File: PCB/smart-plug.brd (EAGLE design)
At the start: 85.1 x 77.1 mm, 10 parts, among them K1 HLS8L-DC3V-S-C, T1 2N2222

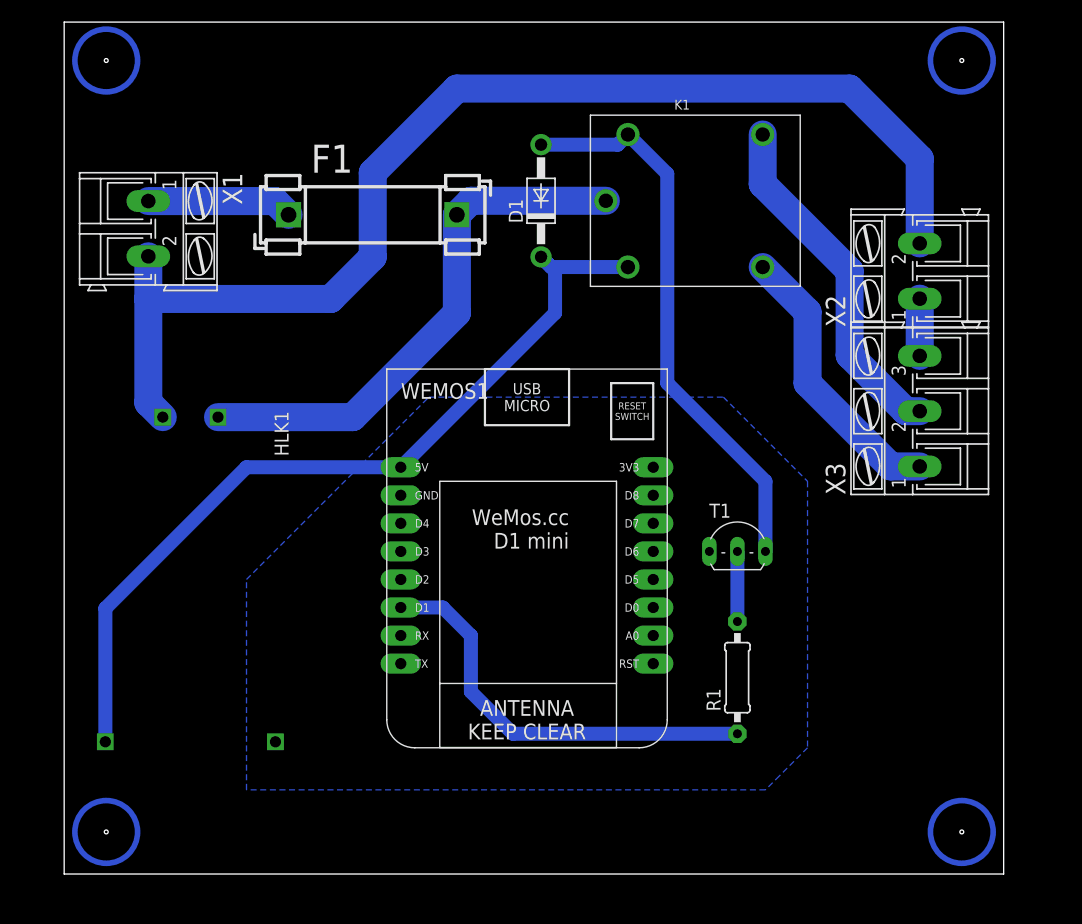
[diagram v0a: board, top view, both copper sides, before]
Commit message: Update files
Added LED indicators
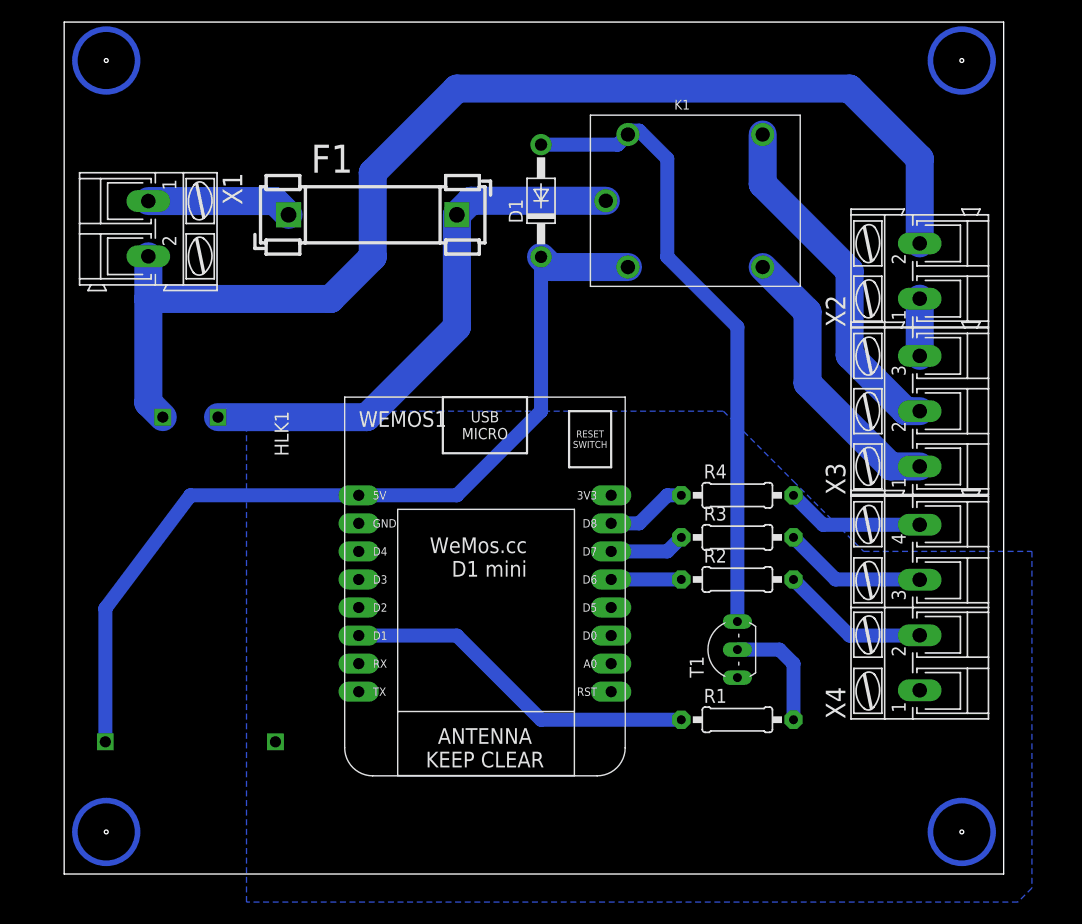
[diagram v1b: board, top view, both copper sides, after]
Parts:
- added R2, R3, R4: (no value), adafruit:0207/10
- added X4: (no value), con-ptr500:AK300/4
- moved T1 10.2 mm to (68.6, 20.3), turned to 90 degrees
- moved WEMOS1 4.58 mm to (48.3, 24.1)
- moved R1 3.81 mm to (69.8, 14.0), turned to 0 degrees
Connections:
- new net LED_BLUE: R4.1, WEMOS1.D8
- new net LED_GREEN: R3.1, WEMOS1.D7
- new net LED_RED: R2.1, WEMOS1.D6
- new net N$10: R4.2, X4.4
- new net N$11: R3.2, X4.3
- new net N$9: R2.2, X4.2
- net AGND: now also X4.1
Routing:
- net N$9: track 0.00 -> 13.5 mm
- net N$11: track 0.00 -> 13.0 mm
- net N$10: track 0.00 -> 12.5 mm
- net LED_BLUE: track 0.00 -> 7.40 mm
- net LED_GREEN: track 0.00 -> 6.88 mm
- net N$6: track 51.2 -> 57.5 mm
- net LED_RED: track 0.00 -> 6.35 mm
- net N$2: track 38.2 -> 32.4 mm
- net N$3: track 6.35 -> 10.7 mm
- net N$4: track 77.7 -> 82.0 mm
- net 220V+: track 48.4 -> 49.2 mm
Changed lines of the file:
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@@
 <attribute name="MPN" value="HLS8L-DC3V-S-C" x="66.04" y="60.96" size="1.778" layer="27" display="off"/>
 </element>
-<element name="R1" library="adafruit" package="0207/10" value="" x="69.85" y="17.78" rot="R90"/>
-<element name="T1" library="adafruit" package="TO92-EBC-OVAL" value="2N2222" x="69.85" y="30.48"/>
-<element name="WEMOS1" library="esp8266modules" package="WEMOS-D1-MINI" value="" x="52.07" y="26.67" rot="R180"/>
+<element name="R1" library="adafruit" package="0207/10" value="" x="69.85" y="13.97"/>
+<element name="T1" library="adafruit" package="TO92-EBC-OVAL" value="2N2222" x="68.58" y="20.32" rot="R90"/>
+<element name="WEMOS1" library="esp8266modules" package="WEMOS-D1-MINI" value="" x="48.26" y="24.13" rot="R180"/>
 <element name="X1" library="con-ptr500" library_urn="urn:adsk.eagle:library:181" package="AK300/2" package3d_urn="urn:adsk.eagle:package:9881/1" value="" x="16.51" y="58.42" rot="R270">
 <attribute name="MF" value="" x="16.51" y="58.42" size="1.778" layer="27" rot="R270" display="off"/>
@@
 <attribute name="OC_NEWARK" value="unknown" x="29.21" y="59.69" size="1.778" layer="27" display="off"/>
 </element>
+<element name="R2" library="adafruit" package="0207/10" value="" x="69.85" y="26.67"/>
+<element name="R3" library="adafruit" package="0207/10" value="" x="69.85" y="30.48"/>
+<element name="R4" library="adafruit" package="0207/10" value="" x="69.85" y="34.29"/>
+<element name="X4" library="con-ptr500" library_urn="urn:adsk.eagle:library:181" package="AK300/4" package3d_urn="urn:adsk.eagle:package:9879/1" value="" x="86.36" y="24.13" rot="R90">
+<attribute name="MF" value="" x="86.36" y="24.13" size="1.778" layer="27" rot="R90" display="off"/>
+<attribute name="MPN" value="" x="86.36" y="24.13" size="1.778" layer="27" rot="R90" display="off"/>
+<attribute name="OC_FARNELL" value="unknown" x="86.36" y="24.13" size="1.778" layer="27" rot="R90" display="off"/>
+<attribute name="OC_NEWARK" value="unknown" x="86.36" y="24.13" size="1.778" layer="27" rot="R90" display="off"/>
+</element>
 </elements>
 <signals>
-<signal name="N$2">
-<contactref element="WEMOS1" pad="D1"/>
-<contactref element="R1" pad="1"/>
-<wire x1="39.37" y1="24.13" x2="43.18" y2="24.13" width="1.27" layer="16"/>
-<wire x1="43.18" y1="24.13" x2="45.72" y2="21.59" width="1.27" layer="16"/>
-<wire x1="45.72" y1="21.59" x2="45.72" y2="16.51" width="1.27" layer="16"/>
-<wire x1="45.72" y1="16.51" x2="49.53" y2="12.7" width="1.27" layer="16"/>
-<wire x1="49.53" y1="12.7" x2="69.85" y2="12.7" width="1.27" layer="16"/>
-</signal>
 <signal name="N$3">
 <contactref element="R1" pad="2"/>
 <contactref element="T1" pad="B"/>
-<wire x1="69.85" y1="22.86" x2="69.85" y2="29.21" width="1.27" layer="16"/>
+<wire x1="69.85" y1="20.32" x2="73.66" y2="20.32" width="1.27" layer="16"/>
+<wire x1="73.66" y1="20.32" x2="74.93" y2="19.05" width="1.27" layer="16"/>
+<wire x1="74.93" y1="19.05" x2="74.93" y2="13.97" width="1.27" layer="16"/>
 </signal>
 <signal name="N$4">
@@
 <contactref element="WEMOS1" pad="5V"/>
 <contactref element="HLK1" pad="P$4"/>
-<wire x1="52.07" y1="55.88" x2="52.99" y2="54.96" width="1.27" layer="16"/>
-<wire x1="52.99" y1="54.96" x2="59.94" y2="54.96" width="1.27" layer="16"/>
-<wire x1="39.37" y1="36.83" x2="53.34" y2="50.8" width="1.27" layer="16"/>
-<wire x1="53.34" y1="50.8" x2="53.34" y2="54.61" width="1.27" layer="16"/>
-<wire x1="53.34" y1="54.61" x2="52.07" y2="55.88" width="1.27" layer="16"/>
 <wire x1="12.62" y1="11.97" x2="12.62" y2="24.05" width="1.27" layer="16"/>
-<wire x1="25.4" y1="36.83" x2="39.37" y2="36.83" width="1.27" layer="16"/>
-<wire x1="12.62" y1="24.05" x2="25.4" y2="36.83" width="1.27" layer="16"/>
+<wire x1="12.62" y1="24.05" x2="20.32" y2="34.29" width="1.27" layer="16"/>
+<wire x1="20.32" y1="34.29" x2="35.56" y2="34.29" width="1.27" layer="16"/>
+<wire x1="35.56" y1="34.29" x2="44.45" y2="34.29" width="1.27" layer="16"/>
+<wire x1="44.45" y1="34.29" x2="52.07" y2="41.91" width="1.27" layer="16"/>
+<wire x1="52.07" y1="41.91" x2="52.07" y2="55.88" width="1.27" layer="16"/>
+<wire x1="52.07" y1="55.88" x2="52.99" y2="54.96" width="2.54" layer="16"/>
+<wire x1="52.99" y1="54.96" x2="59.94" y2="54.96" width="2.54" layer="16"/>
 </signal>
 <signal name="AGND">
@@
 <contactref element="WEMOS1" pad="GND"/>
 <contactref element="HLK1" pad="P$3"/>
+<contactref element="X4" pad="1"/>
 <polygon width="0.508" layer="16">
-<vertex x="25.4" y="7.62"/>
-<vertex x="25.4" y="26.67"/>
-<vertex x="41.91" y="43.18"/>
-<vertex x="68.58" y="43.18"/>
-<vertex x="76.2" y="35.56"/>
-<vertex x="76.2" y="11.43"/>
-<vertex x="73.66" y="8.89"/>
-<vertex x="72.39" y="7.62"/>
+<vertex x="25.4" y="41.91"/>
+<vertex x="68.58" y="41.91"/>
+<vertex x="74.93" y="35.56"/>
+<vertex x="81.28" y="29.21"/>
+<vertex x="96.52" y="29.21"/>
+<vertex x="96.52" y="-1.27"/>
+<vertex x="95.25" y="-2.54"/>
+<vertex x="25.4" y="-2.54"/>
 </polygon>
 </signal>
@@
 <wire x1="52.07" y1="66.04" x2="59.02" y2="66.04" width="1.27" layer="16"/>
 <wire x1="59.02" y1="66.04" x2="59.94" y2="66.96" width="1.27" layer="16"/>
-<wire x1="63.5" y1="63.4" x2="59.94" y2="66.96" width="1.27" layer="16"/>
-<wire x1="72.39" y1="29.21" x2="72.39" y2="35.56" width="1.27" layer="16"/>
-<wire x1="72.39" y1="35.56" x2="63.5" y2="44.45" width="1.27" layer="16"/>
-<wire x1="63.5" y1="44.45" x2="63.5" y2="63.4" width="1.27" layer="16"/>
+<wire x1="69.85" y1="49.53" x2="63.5" y2="55.88" width="1.27" layer="16"/>
+<wire x1="63.5" y1="55.88" x2="63.5" y2="64.77" width="1.27" layer="16"/>
+<wire x1="63.5" y1="64.77" x2="60.96" y2="67.31" width="1.27" layer="16"/>
+<wire x1="60.96" y1="67.31" x2="60.29" y2="67.31" width="1.27" layer="16"/>
+<wire x1="60.29" y1="67.31" x2="59.94" y2="66.96" width="1.27" layer="16"/>
+<wire x1="69.85" y1="22.86" x2="69.85" y2="49.53" width="1.27" layer="16"/>
 </signal>
 <signal name="220V+">
@@
 <contactref element="F1" pad="2"/>
 <contactref element="HLK1" pad="P$1"/>
-<wire x1="22.82" y1="41.37" x2="35.02" y2="41.37" width="2.54" layer="16"/>
-<wire x1="35.02" y1="41.37" x2="44.45" y2="50.8" width="2.54" layer="16"/>
-<wire x1="44.45" y1="50.8" x2="44.45" y2="59.69" width="2.54" layer="16"/>
 <wire x1="57.94" y1="60.96" x2="45.72" y2="60.96" width="2.54" layer="16"/>
 <wire x1="45.72" y1="60.96" x2="44.45" y2="59.69" width="2.54" layer="16"/>
+<wire x1="22.82" y1="41.37" x2="36.29" y2="41.37" width="2.54" layer="16"/>
+<wire x1="36.29" y1="41.37" x2="44.45" y2="49.53" width="2.54" layer="16"/>
+<wire x1="44.45" y1="49.53" x2="44.45" y2="59.69" width="2.54" layer="16"/>
 </signal>
 <signal name="220V-">
@@
 <wire x1="76.2" y1="44.45" x2="76.2" y2="50.9" width="2.54" layer="16"/>
 </signal>
+<signal name="LED_BLUE">
+<contactref element="WEMOS1" pad="D8"/>
+<contactref element="R4" pad="1"/>
+<wire x1="64.77" y1="34.29" x2="63.5" y2="34.29" width="1.27" layer="16"/>
+<wire x1="63.5" y1="34.29" x2="60.96" y2="31.75" width="1.27" layer="16"/>
+<wire x1="60.96" y1="31.75" x2="58.42" y2="31.75" width="1.27" layer="16"/>
+</signal>
+<signal name="LED_GREEN">
+<contactref element="WEMOS1" pad="D7"/>
+<contactref element="R3" pad="1"/>
+<wire x1="64.77" y1="30.48" x2="63.5" y2="29.21" width="1.27" layer="16"/>
+<wire x1="63.5" y1="29.21" x2="58.42" y2="29.21" width="1.27" layer="16"/>
+</signal>
+<signal name="LED_RED">
+<contactref element="WEMOS1" pad="D6"/>
+<contactref element="R2" pad="1"/>
+<wire x1="64.77" y1="26.67" x2="58.42" y2="26.67" width="1.27" layer="16"/>
+</signal>
+<signal name="N$2">
+<contactref element="WEMOS1" pad="D1"/>
+<contactref element="R1" pad="1"/>
+<wire x1="35.56" y1="21.59" x2="44.45" y2="21.59" width="1.27" layer="16"/>
+<wire x1="44.45" y1="21.59" x2="52.07" y2="13.97" width="1.27" layer="16"/>
+<wire x1="52.07" y1="13.97" x2="64.77" y2="13.97" width="1.27" layer="16"/>
+</signal>
+<signal name="N$11">
+<contactref element="X4" pad="3"/>
+<contactref element="R3" pad="2"/>
+<wire x1="86.36" y1="26.6446" x2="86.3346" y2="26.67" width="1.27" layer="16"/>
+<wire x1="78.74" y1="26.67" x2="74.93" y2="30.48" width="1.27" layer="16"/>
+<wire x1="86.3346" y1="26.67" x2="78.74" y2="26.67" width="1.27" layer="16"/>
+</signal>
+<signal name="N$9">
+<contactref element="X4" pad="2"/>
+<contactref element="R2" pad="2"/>
+<wire x1="74.93" y1="26.67" x2="80.01" y2="21.59" width="1.27" layer="16"/>
+<wire x1="80.01" y1="21.59" x2="86.3346" y2="21.59" width="1.27" layer="16"/>
+<wire x1="86.3346" y1="21.59" x2="86.36" y2="21.6154" width="1.27" layer="16"/>
+</signal>
+<signal name="N$10">
+<contactref element="X4" pad="4"/>
+<contactref element="R4" pad="2"/>
+<wire x1="86.36" y1="31.623" x2="77.597" y2="31.623" width="1.27" layer="16"/>
+<wire x1="77.597" y1="31.623" x2="74.93" y2="34.29" width="1.27" layer="16"/>
+</signal>
 </signals>

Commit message: Update files
Added on board LEDs, updated design
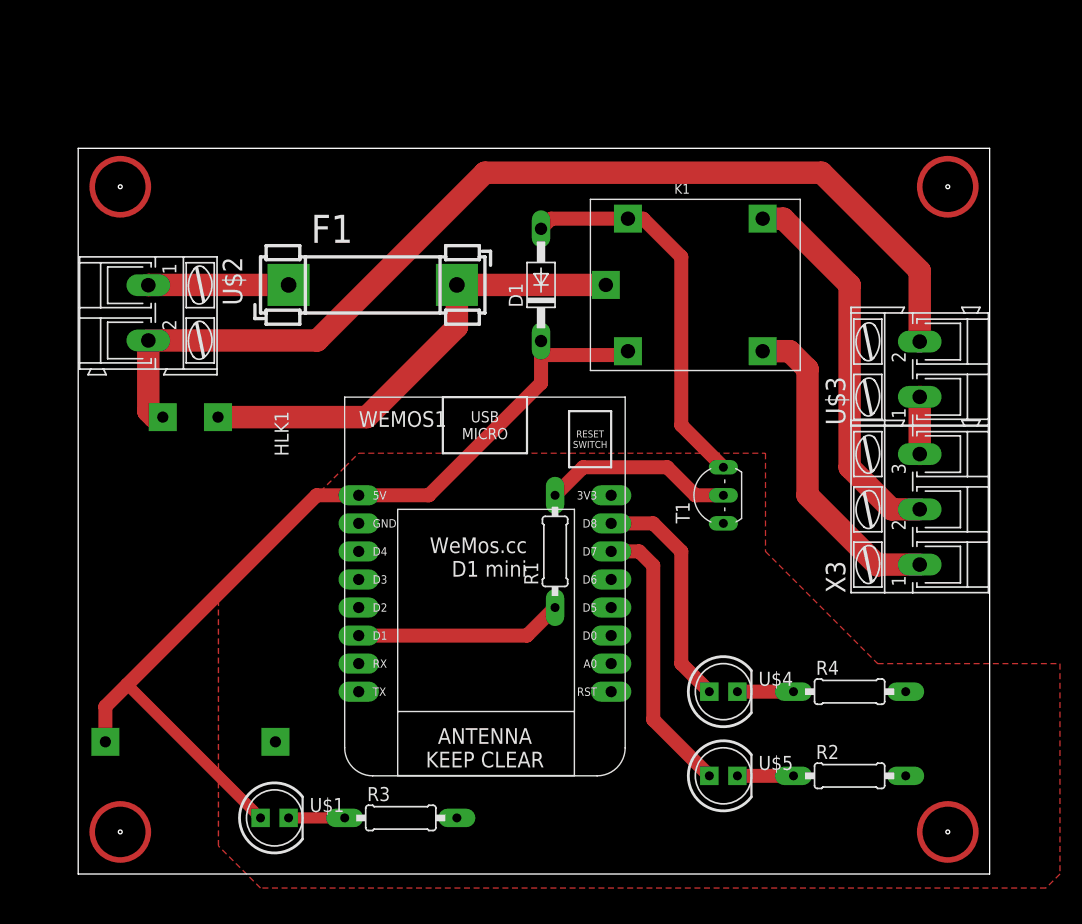
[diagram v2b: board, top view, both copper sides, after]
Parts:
- removed X1, X2: (no value), con-ptr500:AK300/2
- removed X4: (no value), con-ptr500:AK300/4
- added U$1, U$4, U$5: LED5MM, smartplug-components:LED5MM
- added U$2, U$3: OUT-2PINS, smartplug-components:AK300/2
- D1: value 1N4004 -> DIODE; device adafruit:DO41-10 -> smartplug-components:DO41-10
- F1: value FUSEBLANK_5X20MM -> FUSE-HOLDER; device fuse:FUSE_HOLDER_5X20MM -> smartplug-components:FUSE_HOLDER_5X20MM
- HLK1: value HLK-PM013W -> HLK-SUPPLY; device HLK-PM01:HLK-PM01 -> smartplug-components:HLK-PM01
- K1: device Seeed-Relay:REY5-19.0X15.0X15.0MM -> smartplug-components:REY5-19.0X15.0X15.0MM
- R1, R2, R3, R4: value (none) -> RESISTOR; device adafruit:0207/10 -> smartplug-components:0207/10
- WEMOS1: value (none) -> WEMOS-D1-MINI; device esp8266modules:WEMOS-D1-MINI -> smartplug-components:WEMOS-D1-MINI
- X3: value (none) -> OUT-3PINS; device con-ptr500:AK300/3 -> smartplug-components:AK300/3
- moved R3 39.7 mm to (39.4, 5.08)
- moved R1 22.5 mm to (53.3, 29.2), turned to 90 degrees
- moved R2 20.5 mm to (80.0, 8.89)
- moved R4 20.5 mm to (80.0, 16.5)
- moved T1 14.0 mm to (67.3, 34.3)
- moved X3 8.89 mm to (86.4, 33.0)
- moved D1 7.62 mm to (52.1, 53.3)
- moved K1 7.62 mm to (66.0, 53.3)
- moved F1 6.35 mm to (29.2, 53.3)
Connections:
- net N$5 renamed RELAY2
- net N$7 renamed RELAY1
- removed net N$1: X2.1, X3.3
- removed net N$11: R3.2, X4.3
- new net SWITCH: U$3.1, X3.3
- net 220V-: now also U$2.2, U$3.2; no longer X1.2, X2.2
- net AGND: now also R2.2, R3.2, R4.2; no longer X4.1
- net LED_BLUE: now also U$4.A; no longer R4.1
- net LED_GREEN: now also U$1.K; no longer WEMOS1.D7
- net LED_RED: now also U$5.A, WEMOS1.D7; no longer R2.1, WEMOS1.D6
- net N$10: now also R4.1, U$4.K; no longer R4.2, X4.4
- net N$4: now also U$1.A
- net N$8: now also U$2.1; no longer X1.1
- net N$9: now also R2.1, U$5.K; no longer R2.2, X4.2
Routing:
- net N$6: track 57.5 -> 35.1 mm
- net LED_RED: track 6.35 -> 25.5 mm
- net LED_BLUE: track 7.40 -> 21.2 mm
- net N$2: track 32.4 -> 18.8 mm
- net 220V-: track 107.6 -> 94.2 mm
- net N$11: track 13.0 -> 0.00 mm
- net N$9: track 13.5 -> 5.08 mm
- net N$10: track 12.5 -> 5.08 mm
- net 220V+: track 49.2 -> 42.3 mm
- net N$3: track 10.7 -> 17.3 mm
- net SWITCH: track 0.00 -> 5.18 mm
- net N$1: track 5.18 -> 0.00 mm
- net RELAY1: track 25.5 -> 29.0 mm
- net RELAY2: track 31.7 -> 34.8 mm
- net LED_GREEN: track 6.88 -> 5.08 mm
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- added copper zone on layer 1, net AGND
- removed copper zone on layer 16, net AGND
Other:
- board size 85.1 x 77.1 mm -> 82.5 x 65.7 mm

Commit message: Update files
Removed fuse and made PCB smaller
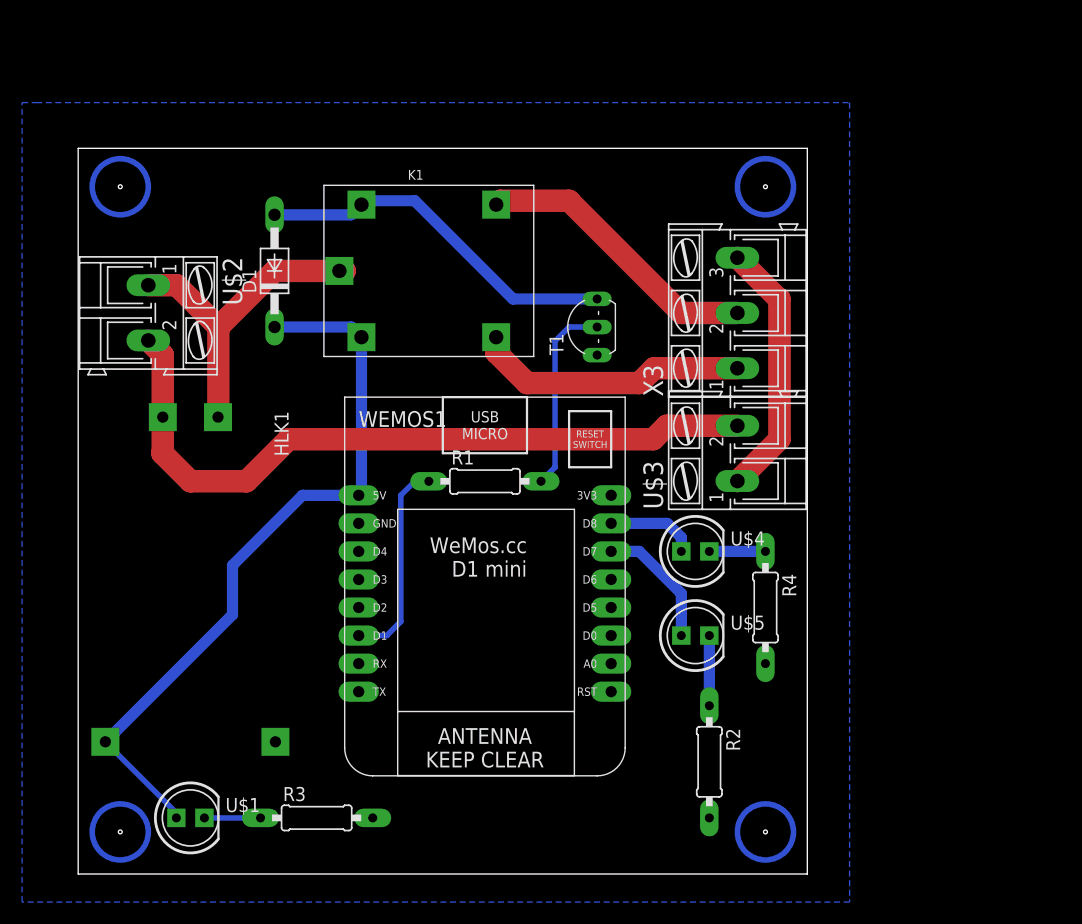
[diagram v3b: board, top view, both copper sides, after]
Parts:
- removed F1: FUSE-HOLDER, smartplug-components:FUSE_HOLDER_5X20MM
- moved X3 24.3 mm to (69.8, 50.8)
- moved K1 24.2 mm to (41.9, 54.6)
- moved D1 24.2 mm to (27.9, 54.6)
- moved T1 19.1 mm to (55.9, 49.5)
- moved U$3 18.2 mm to (69.8, 38.1)
- moved U$4 13.0 mm to (66.0, 29.2)
- moved U$5 13.0 mm to (66.0, 21.6)
- moved R2 12.8 mm to (67.3, 10.2), turned to 270 degrees
- moved R4 10.8 mm to (72.4, 24.1), turned to 270 degrees
- moved R1 8.98 mm to (47.0, 35.6), turned to 0 degrees
- moved U$1 7.62 mm to (20.3, 5.08)
- moved R3 7.62 mm to (31.8, 5.08)
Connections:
- removed net N$8: F1.1, U$2.1
- net 220V+: now also U$2.1; no longer F1.2
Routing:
- net 220V-: track 94.2 -> 66.0 mm
- net SWITCH: track 5.18 -> 23.4 mm
- net N$4: track 83.7 -> 67.0 mm
- net LED_RED: track 25.5 -> 11.7 mm
- net LED_BLUE: track 21.2 -> 8.15 mm
- net N$8: track 12.7 -> 0.00 mm
- net 220V+: track 42.3 -> 30.1 mm
- net RELAY2: track 34.8 -> 26.2 mm
- net RELAY1: track 29.0 -> 24.9 mm
- net N$6: track 35.1 -> 33.4 mm
- net N$9: track 5.08 -> 6.35 mm
- added copper zone on layer 16, net AGND
- removed copper zone on layer 1, net AGND
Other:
- board size 82.5 x 65.7 mm -> 66 x 65.7 mm
- board text added: "BLUE"
- board text added: "GREEN"
- board text added: "LOAD+"
- board text added: "LOAD-"
- board text added: "RED"
- board text added: "SWITCH A"
- board text added: "SWITCH B"
- board text added: "SWITCH COMMON"
